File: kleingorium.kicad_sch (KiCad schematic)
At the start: 18 parts, among them J1 4017 Pins, J10 VCC, J11 GND, J12 4046 Comp In, J2 4040 Output, J3 4040 Input, J4 4046 Out, J5 4046 Comp, J6 Select, J7 Output, J8 Input, J9 4046 SigIn, Q1 2N3904, SW1 4017 Feedback, SW2 4046 CompIn, SW3 Chain

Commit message: after main routing
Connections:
- net 4053/C: now also J7.2 (Pin_2), SW3.2 (B)
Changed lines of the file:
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@@
+	)
+	(junction
+		(at 91.44 175.26)
+		(diameter 0)
+		(color 0 0 0 0)
 	)
 	(junction
@@
 	)
 	(junction
+		(at 104.14 175.26)
+		(diameter 0)
+		(color 0 0 0 0)
+	)
+	(junction
 		(at 254 236.22)
 		(diameter 0)
@@
 		)
 		(stroke
+			(width 0)
+			(type default)
+		)
+	)
+	(wire
+		(pts
+			(xy 91.44 175.26) (xy 104.14 175.26)
+		)
+		(stroke

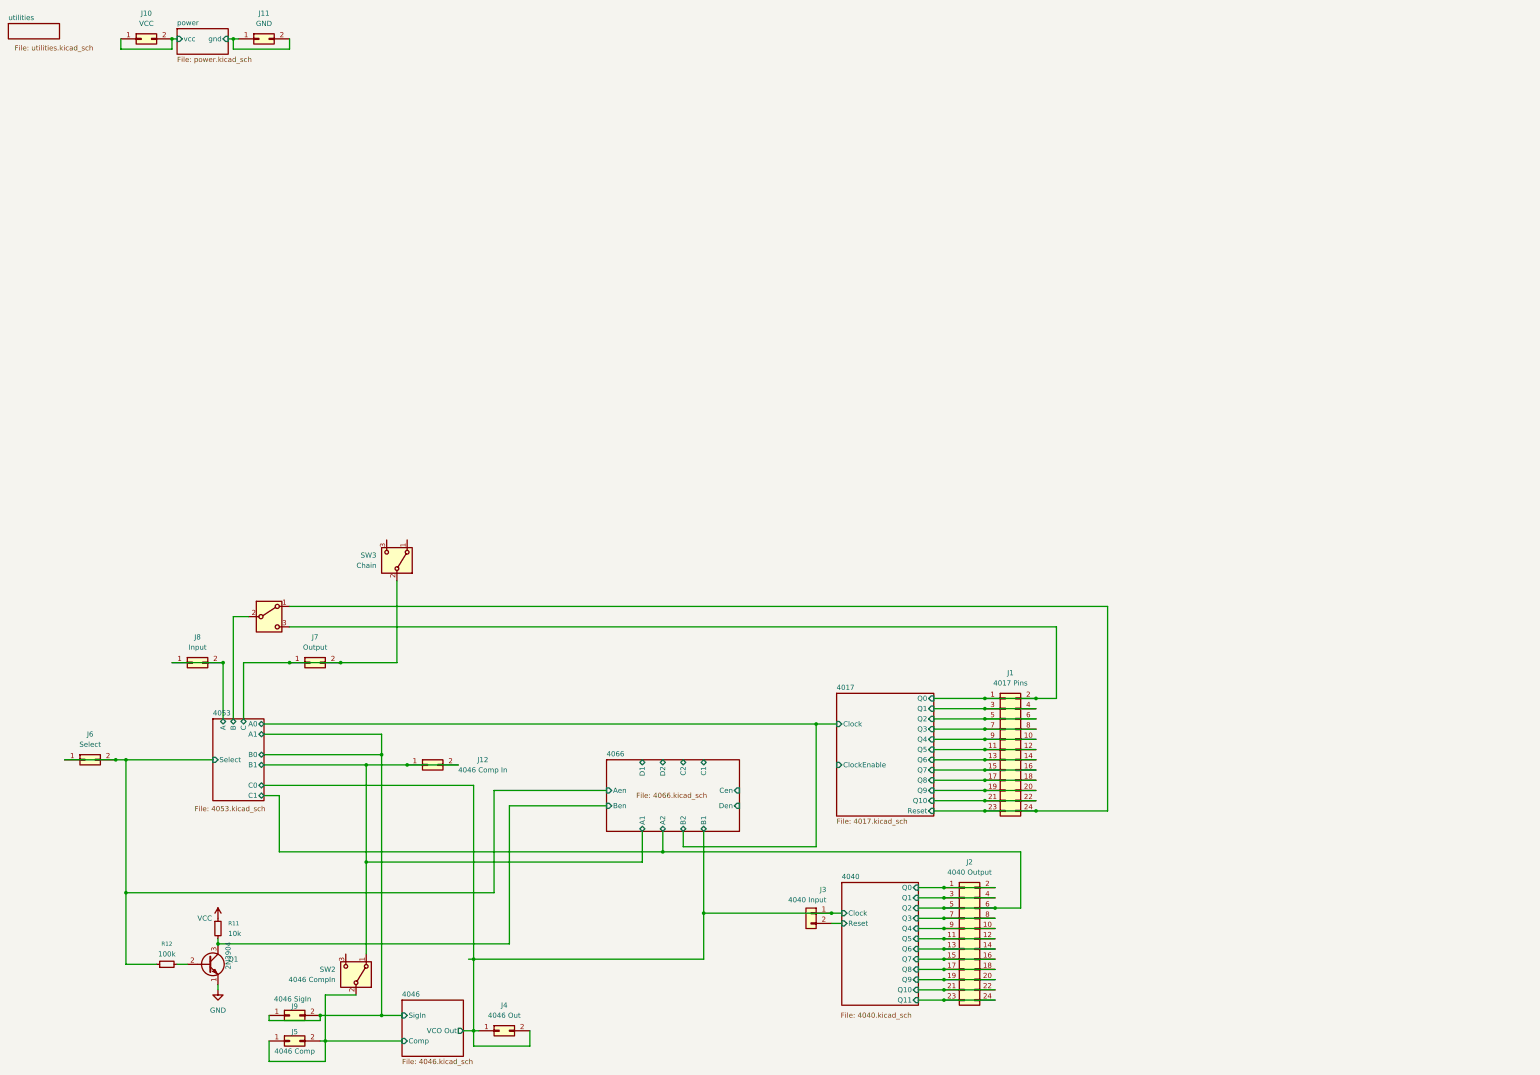
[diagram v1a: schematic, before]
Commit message: schematic doubling without pcb placing
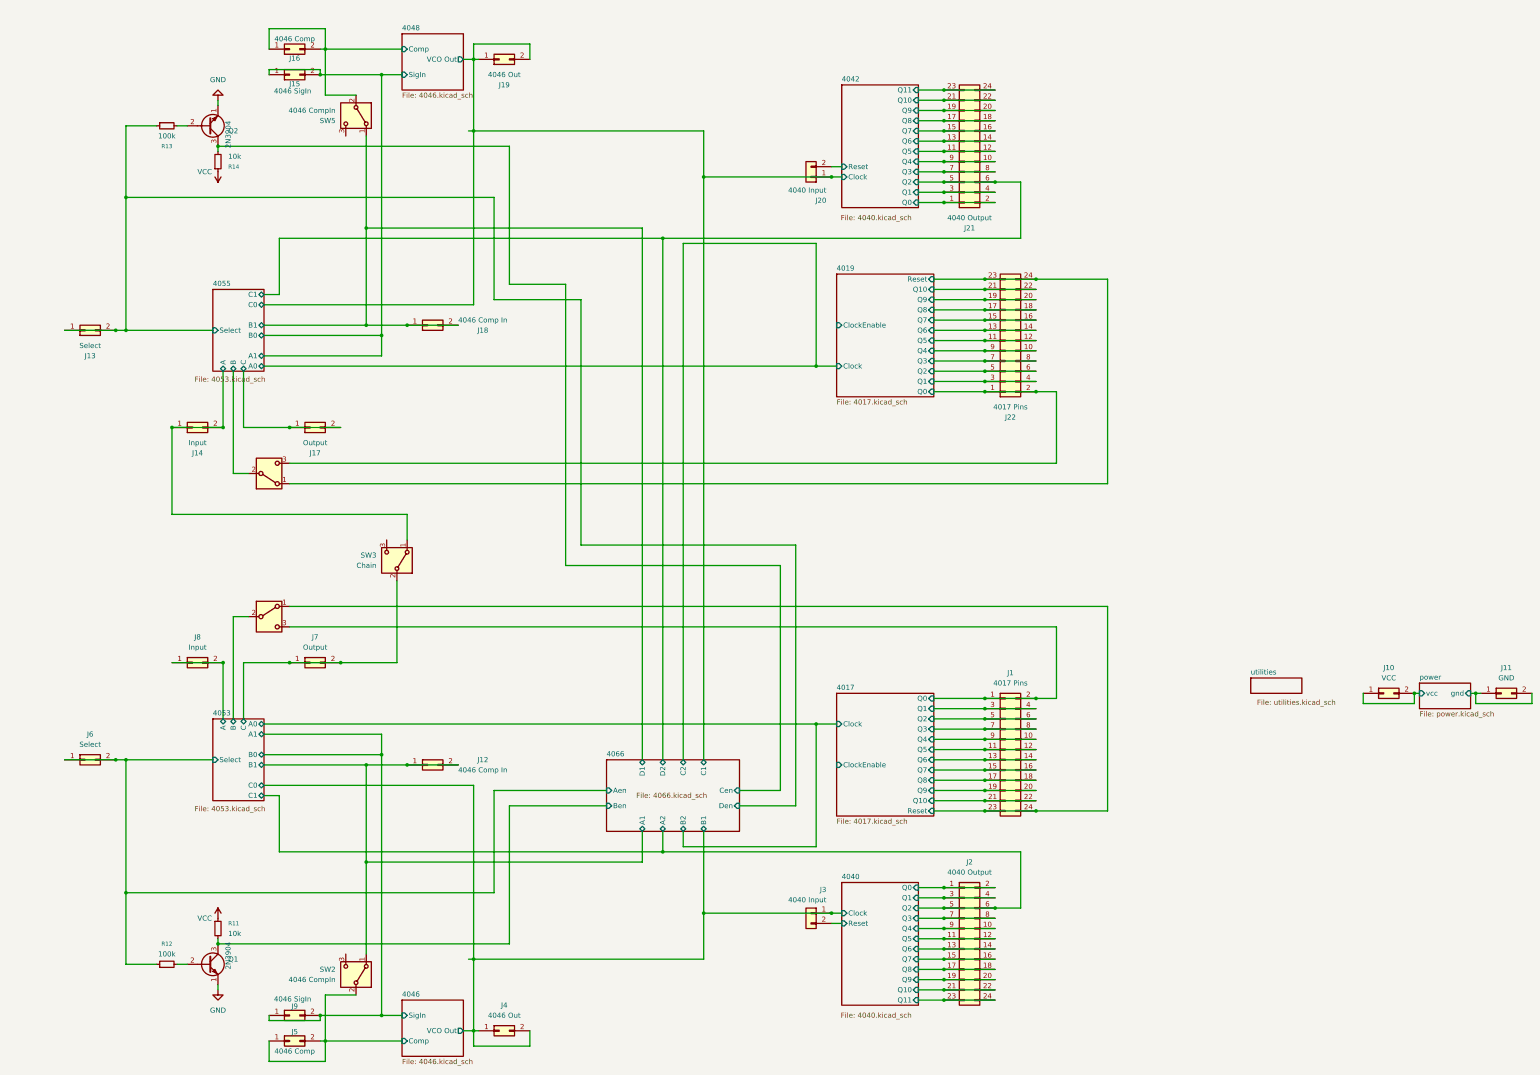
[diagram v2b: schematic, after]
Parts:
- added J13: Select, Connector_PinHeader_2.54mm:PinHeader_2x01_P2.54mm_Vertical, symbol Connector_Generic:Conn_02x01
- added J14: Input, Connector_PinHeader_2.54mm:PinHeader_2x01_P2.54mm_Vertical, symbol Connector_Generic:Conn_02x01
- added J15: 4046 SigIn, Connector_PinHeader_2.54mm:PinHeader_2x01_P2.54mm_Vertical, symbol Connector_Generic:Conn_02x01
- added J16: 4046 Comp, Connector_PinHeader_2.54mm:PinHeader_2x01_P2.54mm_Vertical, symbol Connector_Generic:Conn_02x01
- added J17: Output, Connector_PinHeader_2.54mm:PinHeader_2x01_P2.54mm_Vertical, symbol Connector_Generic:Conn_02x01
- added J18: 4046 Comp In, Connector_PinHeader_2.54mm:PinHeader_2x01_P2.54mm_Vertical, symbol Connector_Generic:Conn_02x01
- added J19: 4046 Out, Connector_PinHeader_2.54mm:PinHeader_2x01_P2.54mm_Vertical, symbol Connector_Generic:Conn_02x01
- added J20: 4040 Input, Connector_PinHeader_2.54mm:PinHeader_1x02_P2.54mm_Vertical, symbol Connector_Generic:Conn_01x02
- added J21: 4040 Output, Connector_PinHeader_2.54mm:PinHeader_2x12_P2.54mm_Vertical, symbol Connector_Generic:Conn_02x12_Odd_Even
- added J22: 4017 Pins, Connector_PinHeader_2.54mm:PinHeader_2x12_P2.54mm_Vertical, symbol Connector_Generic:Conn_02x12_Odd_Even
- added Q2: 2N3904, Package_TO_SOT_THT:TO-92_Inline_Wide, symbol Transistor_BJT:2N3904
- added R13: 100k, Resistor_THT:R_Axial_DIN0207_L6.3mm_D2.5mm_P10.16mm_Horizontal, symbol Device:R_Small
- added R14: 10k, Resistor_THT:R_Axial_DIN0207_L6.3mm_D2.5mm_P10.16mm_Horizontal, symbol Device:R_Small
- added SW4: 4017 Feedback, Button_Switch_THT:SW_CK_JS202011CQN_DPDT_Straight, symbol Switch:SW_DPDT_x2
- added SW5: 4046 CompIn, Button_Switch_THT:SW_E-Switch_EG1271_SPDT, symbol Switch:SW_SPDT
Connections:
- net 4066/Cen: now also Q2.3 (C), R14.2
- net GND: now also Q2.1 (E)
- net VCC: now also R14.1
- net 4055/A: now reaches SW3.1 (A)
- net 4055/A: now also J14.1 (Pin_1), J14.2 (Pin_2)
- new net: Q2.2 (B), R13.2
- new net 4019/Q0: J22.1 (Pin_1), J22.2 (Pin_2), SW4.3 (C)
- new net 4019/Q1: J22.3 (Pin_3), J22.4 (Pin_4)
- new net 4019/Q10: J22.21 (Pin_21), J22.22 (Pin_22)
- new net 4019/Q2: J22.5 (Pin_5), J22.6 (Pin_6)
- new net 4019/Q3: J22.7 (Pin_7), J22.8 (Pin_8)
- new net 4019/Q4: J22.10 (Pin_10), J22.9 (Pin_9)
- new net 4019/Q5: J22.11 (Pin_11), J22.12 (Pin_12)
- new net 4019/Q6: J22.13 (Pin_13), J22.14 (Pin_14)
- new net 4019/Q7: J22.15 (Pin_15), J22.16 (Pin_16)
- new net 4019/Q8: J22.17 (Pin_17), J22.18 (Pin_18)
- new net 4019/Q9: J22.19 (Pin_19), J22.20 (Pin_20)
- new net 4019/Reset: J22.23 (Pin_23), J22.24 (Pin_24), SW4.1 (A)
- new net 4042/Clock: J19.1 (Pin_1), J19.2 (Pin_2), J20.1 (Pin_1)
- new net 4042/Q0: J21.1 (Pin_1), J21.2 (Pin_2)
- new net 4042/Q1: J21.3 (Pin_3), J21.4 (Pin_4)
- new net 4042/Q10: J21.21 (Pin_21), J21.22 (Pin_22)
- new net 4042/Q11: J21.23 (Pin_23), J21.24 (Pin_24)
- new net 4042/Q2: J21.5 (Pin_5), J21.6 (Pin_6)
- new net 4042/Q3: J21.7 (Pin_7), J21.8 (Pin_8)
- new net 4042/Q4: J21.10 (Pin_10), J21.9 (Pin_9)
- new net 4042/Q5: J21.11 (Pin_11), J21.12 (Pin_12)
- new net 4042/Q6: J21.13 (Pin_13), J21.14 (Pin_14)
- new net 4042/Q7: J21.15 (Pin_15), J21.16 (Pin_16)
- new net 4042/Q8: J21.17 (Pin_17), J21.18 (Pin_18)
- new net 4042/Q9: J21.19 (Pin_19), J21.20 (Pin_20)
- new net 4042/Reset: J20.2 (Pin_2)
- new net 4048/Comp: J16.1 (Pin_1), J16.2 (Pin_2), SW5.2 (B)
- new net 4048/SigIn: J15.1 (Pin_1), J15.2 (Pin_2)
- new net 4055/B: SW4.2 (B)
- new net 4055/B1: J18.1 (Pin_1), J18.2 (Pin_2), SW5.1 (A)
- new net 4055/C: J17.1 (Pin_1), J17.2 (Pin_2)
- new net 4055/Select: J13.1 (Pin_1), J13.2 (Pin_2), R13.1
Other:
- added sheet 4019 (4017.kicad_sch)
- added sheet 4042 (4040.kicad_sch)
- added sheet 4048 (4046.kicad_sch)
- added sheet 4055 (4053.kicad_sch)
- moved on the sheet: J10, J11

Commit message: pcb placing doubling without routing
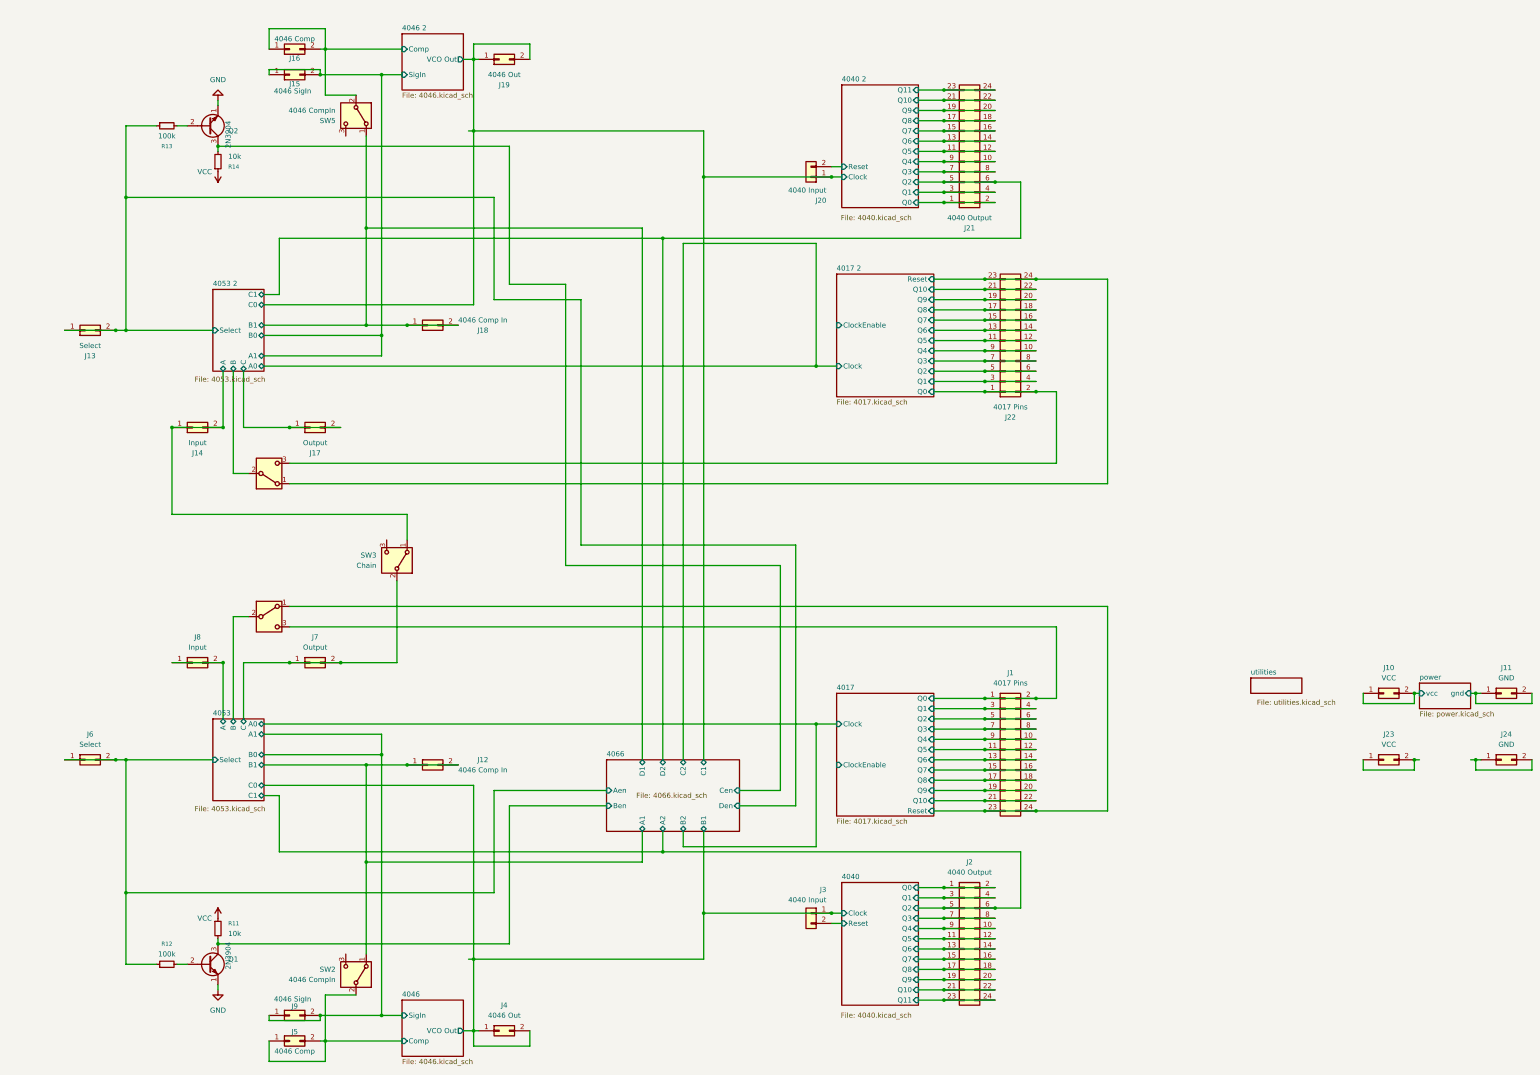
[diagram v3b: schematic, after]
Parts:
- added J23: VCC, Connector_PinHeader_2.54mm:PinHeader_2x01_P2.54mm_Vertical, symbol Connector_Generic:Conn_02x01
- added J24: GND, Connector_PinHeader_2.54mm:PinHeader_2x01_P2.54mm_Vertical, symbol Connector_Generic:Conn_02x01
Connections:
- new net: J24.1 (Pin_1), J24.2 (Pin_2)
- new net: J23.1 (Pin_1), J23.2 (Pin_2)
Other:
- sheet 4019 renamed 4017 2
- sheet 4042 renamed 4040 2
- sheet 4048 renamed 4046 2
- sheet 4055 renamed 4053 2
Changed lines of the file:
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@@
 	)
 	(junction
+		(at 386.08 199.39)
+		(diameter 0)
+		(color 0 0 0 0)
+	)
+	(junction
 		(at 264.16 212.09)
 		(diameter 0)
@@
 	)
 	(junction
+		(at 370.84 199.39)
+		(diameter 0)
+		(color 0 0 0 0)
+	)
+	(junction
 		(at 370.84 182.88)
 		(diameter 0)
@@
 	(wire
 		(pts
+			(xy 400.05 201.93) (xy 386.08 201.93)
+		)
+		(stroke
+			(width 0)
+			(type default)
+		)
+	)
+	(wire
+		(pts
 			(xy 114.3 99.06) (xy 114.3 93.98)
 		)
@@
 	(wire
 		(pts
+			(xy 384.81 199.39) (xy 386.08 199.39)
+		)
+		(stroke
+			(width 0)
+			(type default)
+		)
+	)
+	(wire
+		(pts
 			(xy 110.49 200.66) (xy 120.65 200.66)
 		)
@@
 	(wire
 		(pts
+			(xy 370.84 201.93) (xy 370.84 199.39)
+		)
+		(stroke
+			(width 0)
+			(type default)
+		)
+	)
+	(wire
+		(pts
 			(xy 247.65 248.92) (xy 254 248.92)
 		)
@@
 	(wire
 		(pts
+			(xy 400.05 199.39) (xy 400.05 201.93)
+		)
+		(stroke
+			(width 0)
+			(type default)
+		)
+	)
+	(wire
+		(pts
 			(xy 254 231.14) (xy 266.7 231.14)
 		)
@@
 	(wire
 		(pts
+			(xy 386.08 201.93) (xy 386.08 199.39)
+		)
+		(stroke
+			(width 0)
+			(type default)
+		)
+	)
+	(wire
+		(pts
 			(xy 189.23 71.12) (xy 189.23 199.39)
 		)
@@
 	(wire
 		(pts
+			(xy 358.14 201.93) (xy 370.84 201.93)
+		)
+		(stroke
+			(width 0)
+			(type default)
+		)
+	)
+	(wire
+		(pts
 			(xy 251.46 189.23) (xy 264.16 189.23)
 		)
@@
 	(wire
 		(pts
+			(xy 370.84 199.39) (xy 372.11 199.39)
+		)
+		(stroke
+			(width 0)
+			(type default)
+		)
+	)
+	(wire
+		(pts
 			(xy 184.15 69.85) (xy 273.05 69.85)
 		)
@@
 	(wire
 		(pts
+			(xy 358.14 199.39) (xy 358.14 201.93)
+		)
+		(stroke
+			(width 0)
+			(type default)
+		)
+	)
+	(wire
+		(pts
 			(xy 264.16 201.93) (xy 276.86 201.93)
 		)
@@
 	(wire
 		(pts
+			(xy 386.08 199.39) (xy 387.35 199.39)
+		)
+		(stroke
+			(width 0)
+			(type default)
+		)
+	)
+	(wire
+		(pts
 			(xy 294.64 212.09) (xy 276.86 212.09)
 		)
@@
 	(symbol
 		(lib_id "Connector_Generic:Conn_02x01")
+		(at 392.43 199.39 0)
+		(unit 1)
+		(exclude_from_sim no)
+		(in_bom yes)
+		(on_board yes)
+		(dnp no)
+		(property "Reference" "J24"
+			(at 393.7 193.04 0)
+			(effects
+				(font
+					(size 1.27 1.27)
+				)
+			)
+		)
+		(property "Value" "GND"
+			(at 393.7 195.58 0)
+			(effects
+				(font
+					(size 1.27 1.27)
+				)
+			)
+		)
+		(property "Footprint" "Connector_PinHeader_2.54mm:PinHeader_2x01_P2.54mm_Vertical"
+			(at 392.43 199.39 0)
+			(effects
+				(font
+					(size 1.27 1.27)
+				)
+				(hide yes)
+			)
+		)
+		(property "Datasheet" "~"
+			(at 392.43 199.39 0)
+			(effects
+				(font
+					(size 1.27 1.27)
+				)
+				(hide yes)
+			)
+		)
+		(property "Description" "Generic connector, double row, 02x01, this symbol is compatible with counter-clockwise, top-bottom and odd-even numbering schemes., script generated (kicad-library-utils/schlib/autogen/connector/)"
+			(at 392.43 199.39 0)
+			(effects
+				(font
+					(size 1.27 1.27)
+				)
+				(hide yes)
+			)
+		)
+		(pin "1"
+		)
+		(pin "2"
+		)
+		(instances
+			(project "kleingorium"
+				(path "/01c1f2c1-4d06-4880-847a-9ab55552e3fd"
+					(reference "J24")
+					(unit 1)
+				)
+			)
+		)
+	)
+	(symbol
+		(lib_id "Connector_Generic:Conn_02x01")
 		(at 67.31 116.84 0)
 		(mirror x)
@@
 	(symbol
 		(lib_id "Connector_Generic:Conn_02x01")
+		(at 363.22 199.39 0)
+		(unit 1)
+		(exclude_from_sim no)
+		(in_bom yes)
+		(on_board yes)
+		(dnp no)
+		(fields_autoplaced yes)
+		(property "Reference" "J23"
+			(at 364.49 193.04 0)
+			(effects
+				(font
+					(size 1.27 1.27)
+				)
+			)
+		)
+		(property "Value" "VCC"
+			(at 364.49 195.58 0)
+			(effects
+				(font
+					(size 1.27 1.27)
+				)
+			)
+		)
+		(property "Footprint" "Connector_PinHeader_2.54mm:PinHeader_2x01_P2.54mm_Vertical"
+			(at 363.22 199.39 0)
+			(effects
+				(font
+					(size 1.27 1.27)
+				)
+				(hide yes)
+			)
+		)
+		(property "Datasheet" "~"
+			(at 363.22 199.39 0)
+			(effects
+				(font
+					(size 1.27 1.27)
+				)
+				(hide yes)
+			)
+		)
+		(property "Description" "Generic connector, double row, 02x01, this symbol is compatible with counter-clockwise, top-bottom and odd-even numbering schemes., script generated (kicad-library-utils/schlib/autogen/connector/)"
+			(at 363.22 199.39 0)
+			(effects
+				(font
+					(size 1.27 1.27)
+				)
+				(hide yes)
+			)
+		)
+		(pin "1"
+		)
+		(pin "2"
+		)
+		(instances
+			(project "kleingorium"
+				(path "/01c1f2c1-4d06-4880-847a-9ab55552e3fd"
+					(reference "J23")
+					(unit 1)
+				)
+			)
+		)
+	)
+	(symbol
+		(lib_id "Connector_Generic:Conn_02x01")
 		(at 96.52 116.84 0)
 		(mirror x)
@@
 			(color 0 0 0 0.0000)
 		)
-		(property "Sheetname" "4019"
+		(property "Sheetname" "4017 2"
 			(at 227.33 78.0284 0)
 			(effects
@@
 			(color 0 0 0 0.0000)
 		)
-		(property "Sheetname" "4042"
+		(property "Sheetname" "4040 2"
 			(at 228.6 31.0384 0)
 			(effects
@@
 			(color 0 0 0 0.0000)
 		)
-		(property "Sheetname" "4048"
+		(property "Sheetname" "4046 2"
 			(at 119.38 18.3384 0)
 			(effects
@@
 			(color 0 0 0 0.0000)
 		)
-		(property "Sheetname" "4055"
+		(property "Sheetname" "4053 2"
 			(at 72.39 81.8384 0)
 			(effects
